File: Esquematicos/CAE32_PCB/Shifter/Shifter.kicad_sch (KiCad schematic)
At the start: 20 parts, among them J1 EXP-PORT, J2 SPI_DEVICE, J3 Conn_01x08_Female, J4 Conn_01x08_Female, J5 Conn_01x08_Female, SW1 USB_BOOT, U1 RP2040, U2 W25Q16JVSNIQ, Y1 12Mhz

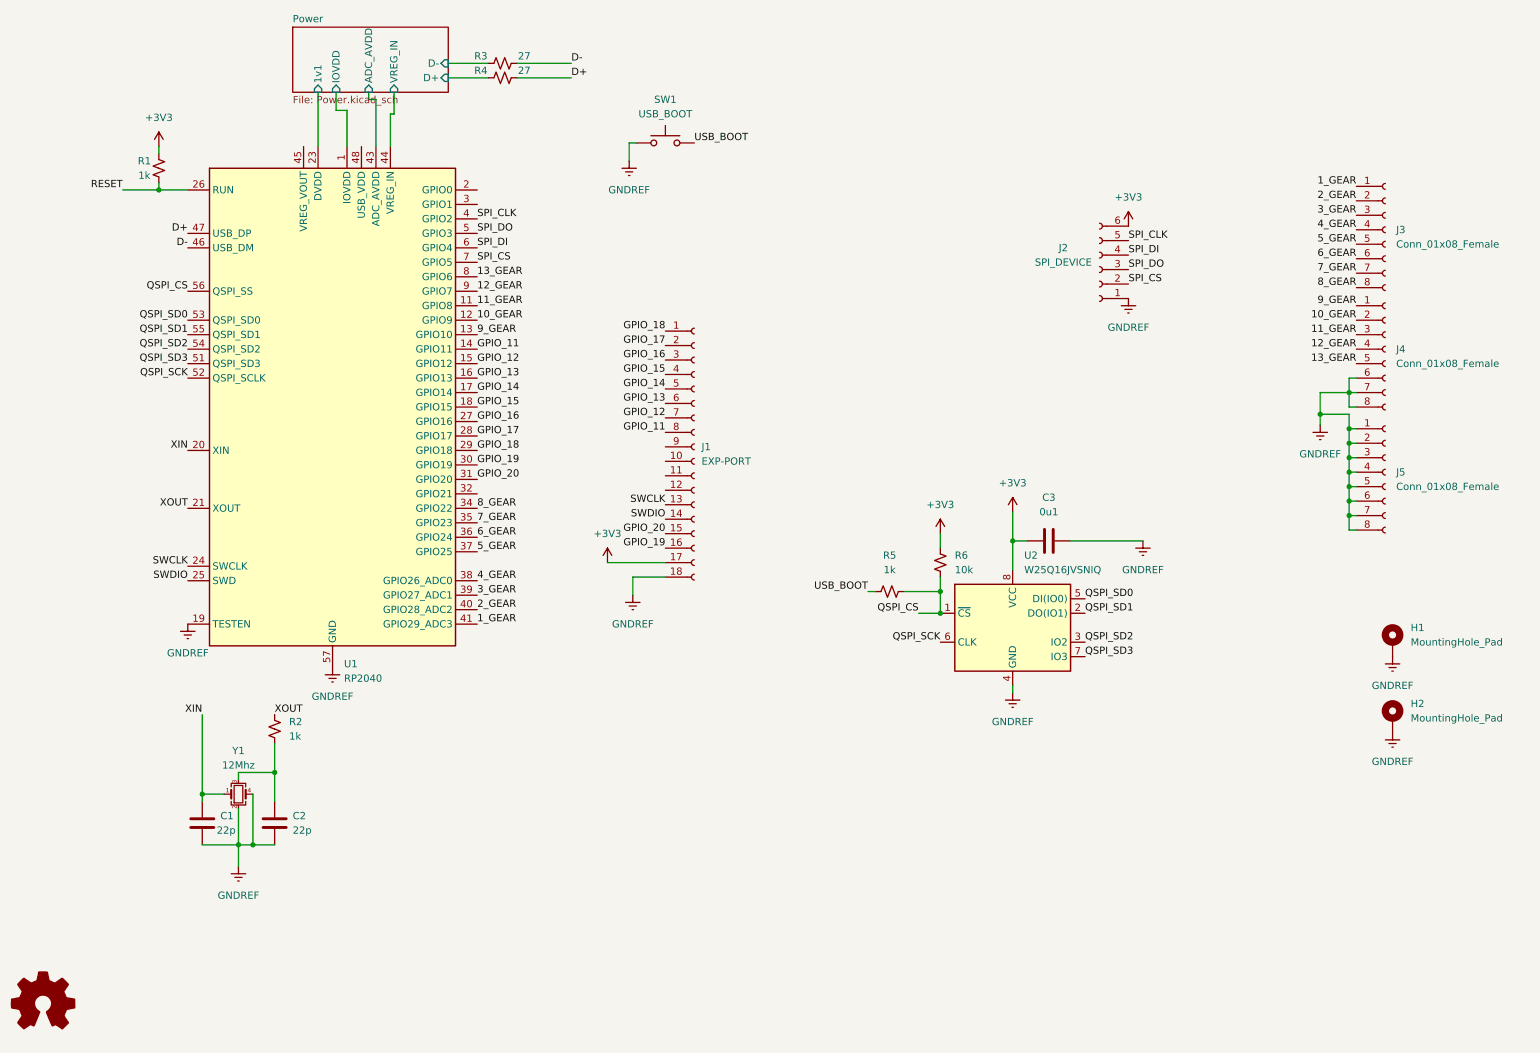
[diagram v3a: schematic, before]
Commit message: update: Se añade nombre y se separa a los diferentes componentes por categoria en el esquematico
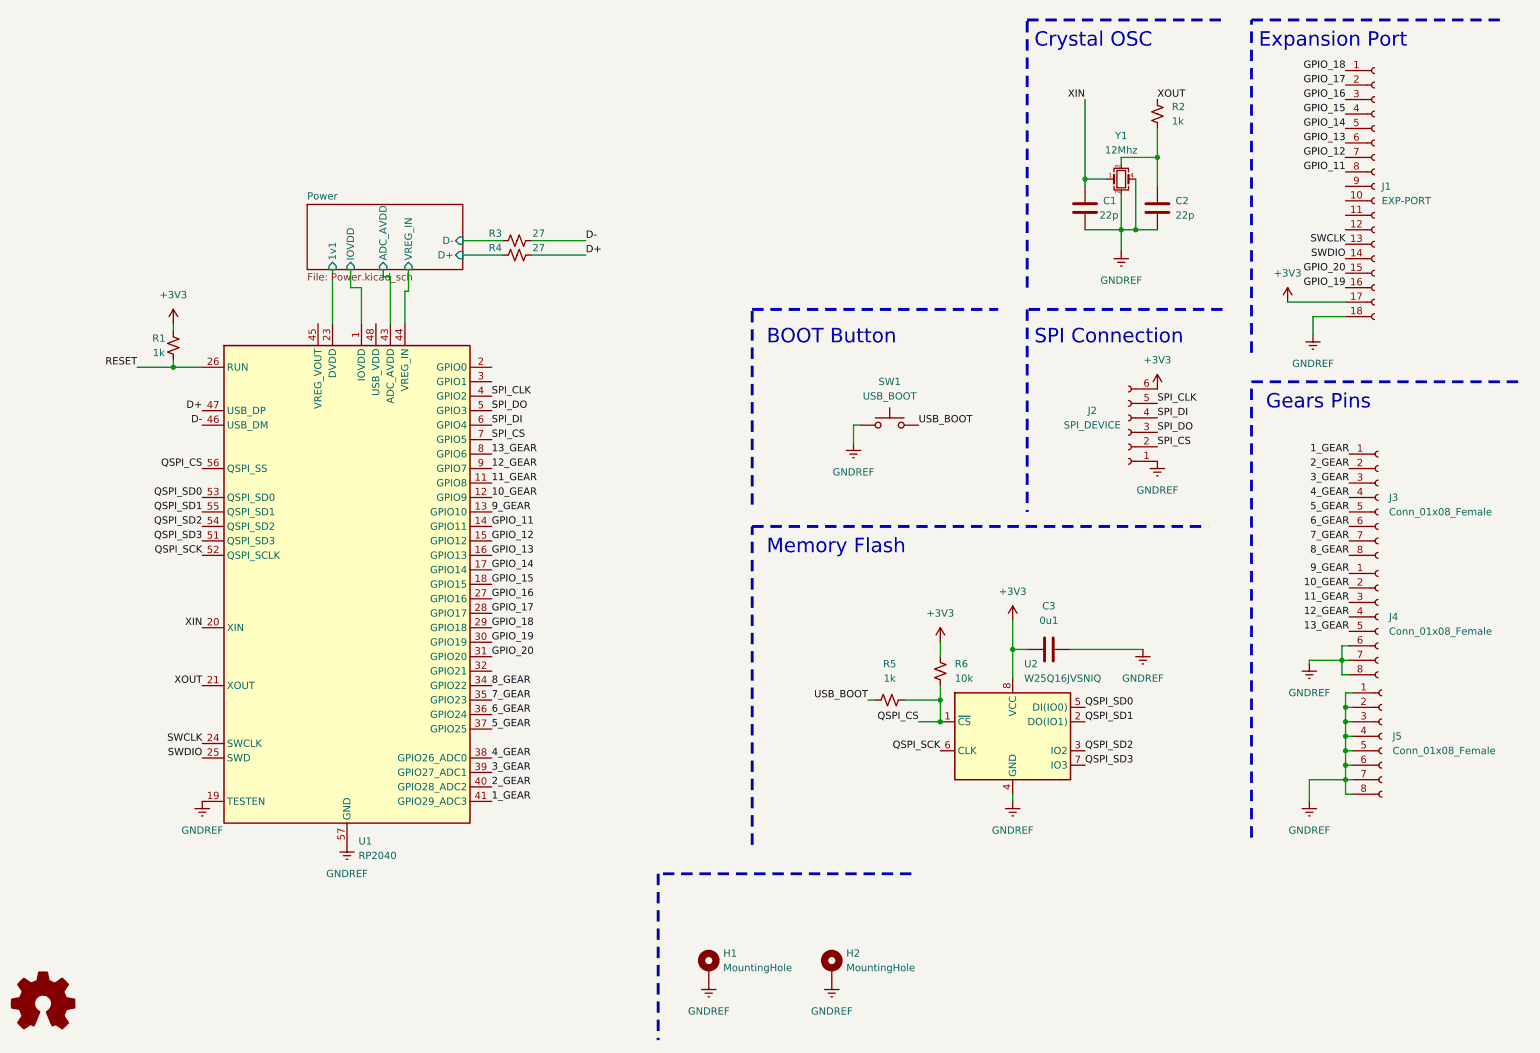
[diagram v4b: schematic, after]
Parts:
- H1, H2: value MountingHole_Pad -> MountingHole
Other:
- note added: "BOOT Button"
- note added: "Crystal OSC"
- note added: "Expansion Port"
- note added: "Gears Pins"
- note added: "Memory Flash"
- note added: "SPI Connection"
- title: (none) -> CAE32 Shifter
- moved on the sheet: C1, C2, C3, H1, H2, J1, J2, J3, J4, J5, R1, R2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

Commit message: update: changed the castelled holes for pin sockets and changed 0603 footprints to 0402
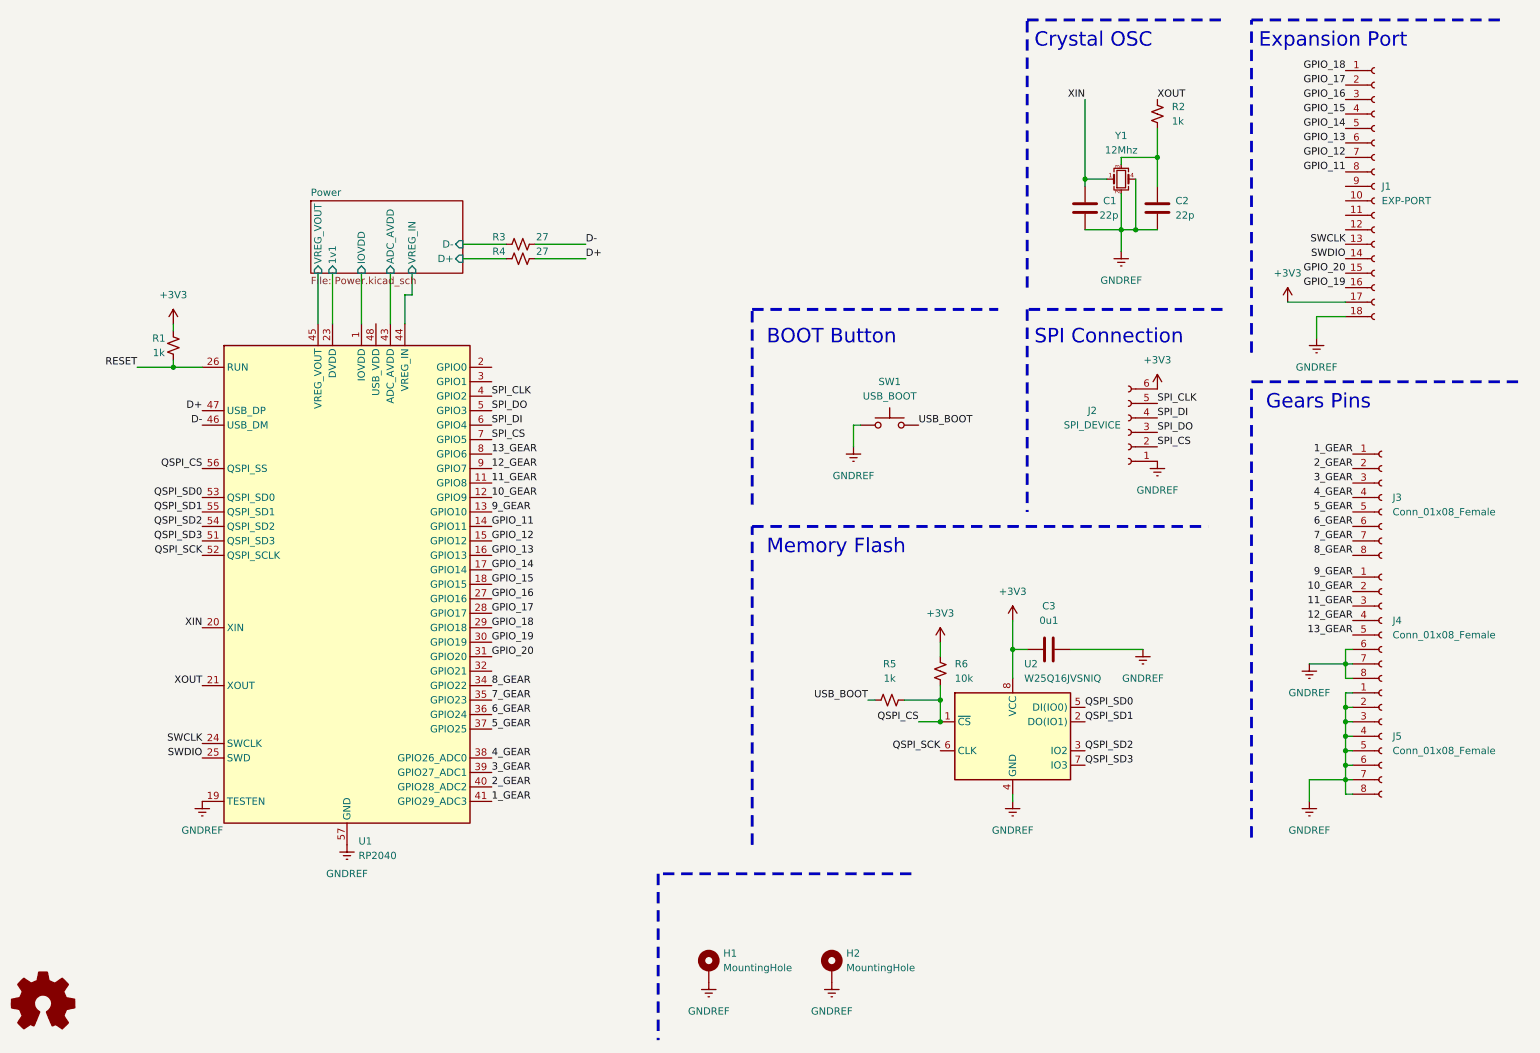
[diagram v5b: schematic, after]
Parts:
- C1, C2, C3: footprint Capacitor_SMD:C_0603_1608Metric_Pad1.08x0.95mm_HandSolder -> Capacitor_SMD:C_01005_0402Metric
- J3, J4, J5: footprint shifter:shi -> Connector_PinSocket_2.54mm:PinSocket_1x08_P2.54mm_Vertical
- R1, R2, R3, R4, R5, R6: footprint Resistor_SMD:R_0603_1608Metric_Pad0.98x0.95mm_HandSolder -> Resistor_SMD:R_0402_1005Metric
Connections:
- net Power/VREG_VOUT: now reaches U1.45 (VREG_VOUT)
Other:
- sheet Power ports: added VREG_VOUT; removed none
- moved on the sheet: J3, J4, R3, R4

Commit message: chore: arrange of schematic elements
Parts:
- C3: Vendor C42998 -> C913620
- J3, J4, J5: Vendor (none) -> C27438
- Y1: Vendor (none) -> C9002
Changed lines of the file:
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@@
+      (effects (font (size 1.27 1.27)) hide)
+    )
+    (property "Vendor" "C9002" (at 210.82 44.45 0)
       (effects (font (size 1.27 1.27)) hide)
     )
@@
       (effects (font (size 1.27 1.27)) hide)
     )
+    (property "Vendor" "C27438" (at 256.54 142.24 0)
+      (effects (font (size 1.27 1.27)) hide)
+    )
     (pin "1")
     (pin "2")
@@
       (effects (font (size 1.27 1.27)) hide)
     )
+    (property "Vendor" "C27438" (at 256.54 100.33 0)
+      (effects (font (size 1.27 1.27)) hide)
+    )
     (pin "1")
     (pin "2")
@@
       (effects (font (size 1.27 1.27)) hide)
     )
+    (property "Vendor" "C27438" (at 256.54 121.92 0)
+      (effects (font (size 1.27 1.27)) hide)
+    )
     (pin "1")
     (pin "2")
@@
       (effects (font (size 1.27 1.27)) hide)
     )
-    (property "Vendor" "C42998" (at 198.12 127 0)
-      (effects (font (size 1.27 1.27)) hide)
-    )
+    (property "Vendor" "C913620" (at 198.12 127 0)
+      (effects (font (size 1.27 1.27)) hide)
+    )

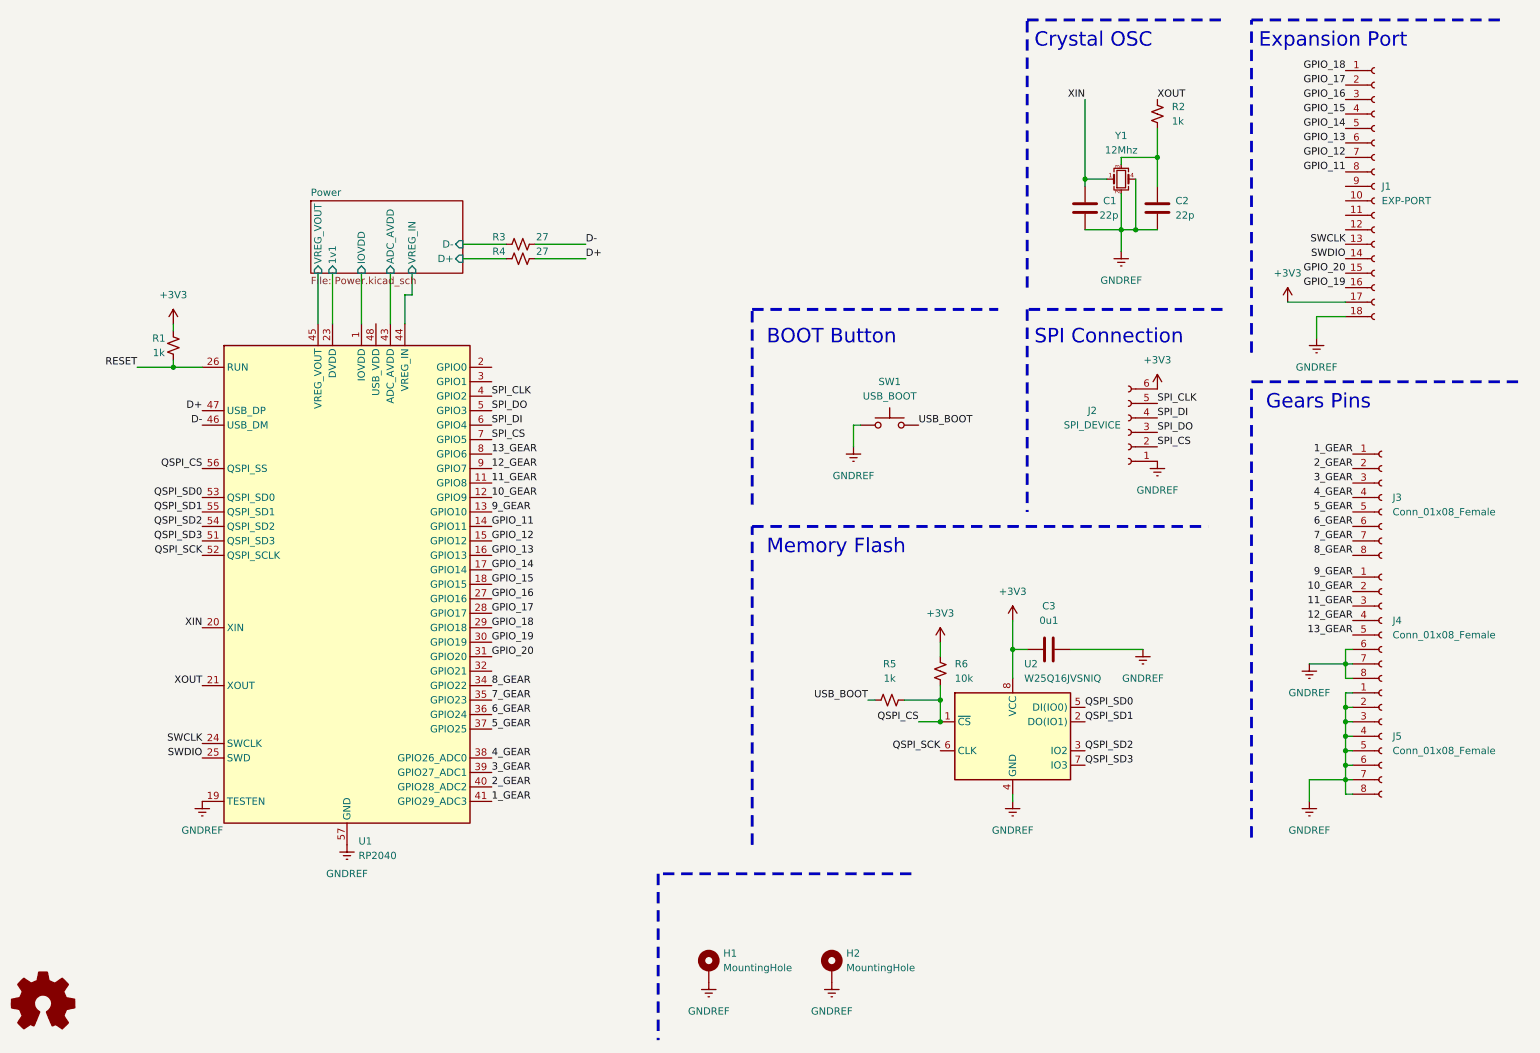
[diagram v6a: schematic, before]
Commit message: update: added minor improvements to Shifter's PCB
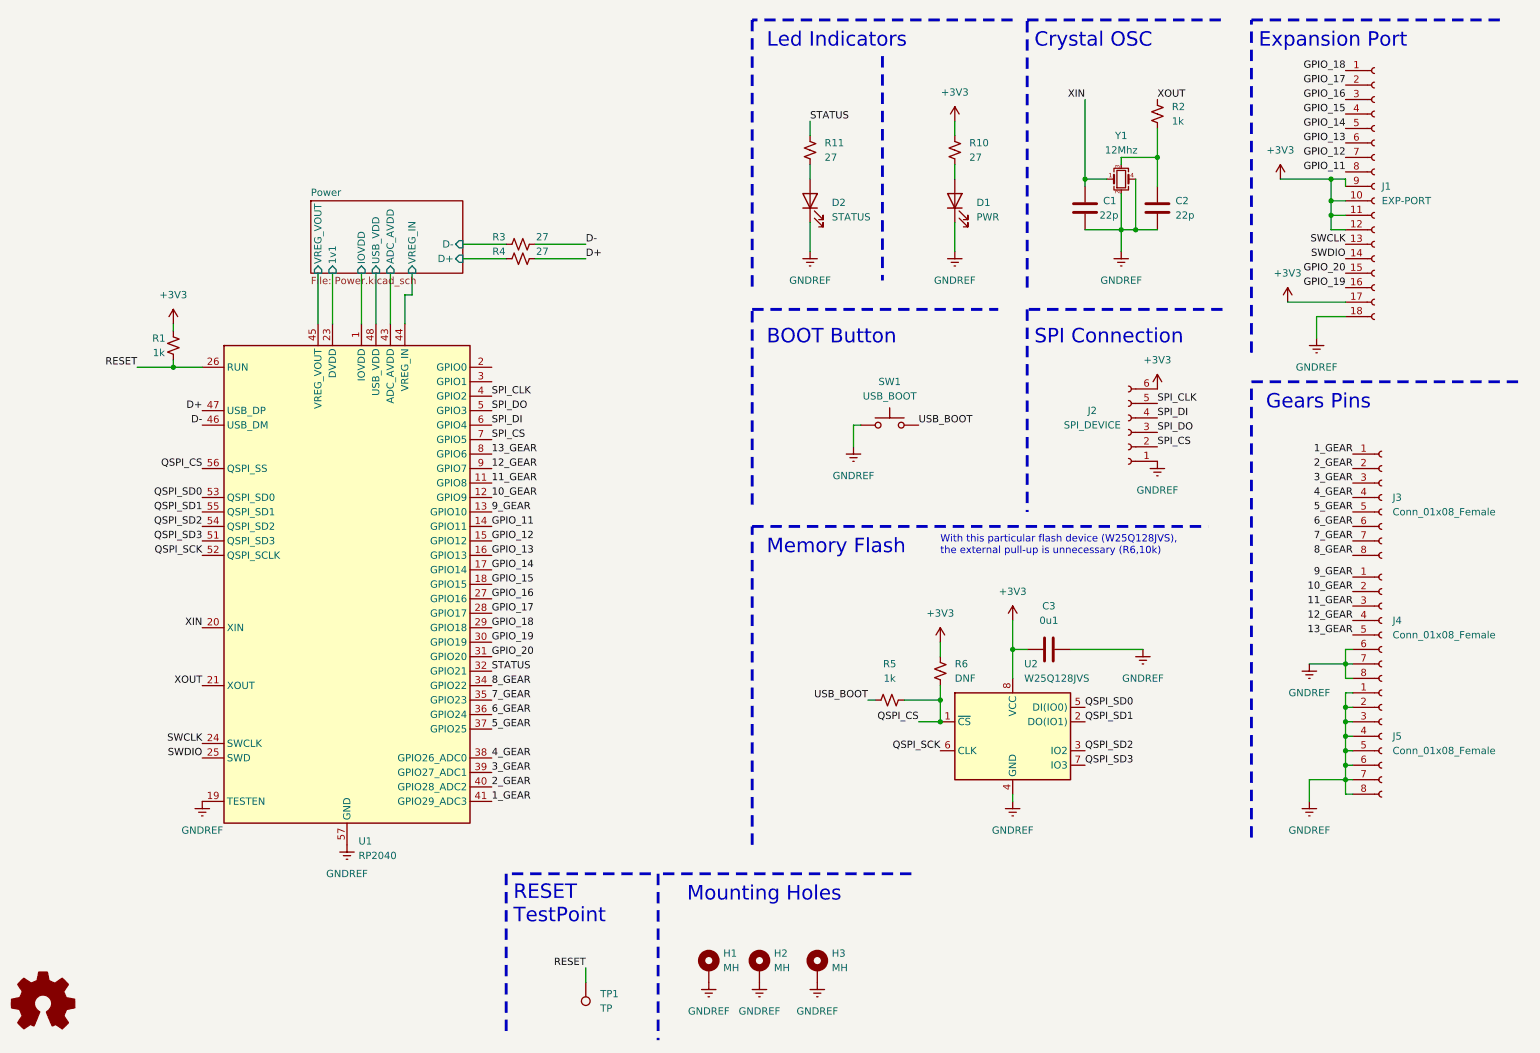
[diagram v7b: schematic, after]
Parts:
- added D1: PWR, LED_SMD:LED_0402_1005Metric, symbol Device:LED
- added D2: STATUS, LED_SMD:LED_0402_1005Metric, symbol Device:LED
- added H3: MH, MountingHole:MountingHole_2.7mm_M2.5_Pad_Via, symbol Mechanical:MountingHole_Pad
- added R10, R11: 27, Resistor_SMD:R_0402_1005Metric, symbol Device:R_Small_US
- added TP1: TP, TestPoint:TestPoint_Pad_D1.0mm, symbol Connector:TestPoint
- H1, H2: value MountingHole -> MH
- R6: value 10k -> DNF
- U2: value W25Q16JVSNIQ -> W25Q128JVS; Vendor C2456211 -> C97521
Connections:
- net +3V3: now also J1.10 (Pin_10), J1.11 (Pin_11), J1.12 (Pin_12), J1.9 (Pin_9), R10.1
- net GNDREF: now also D1.1 (K), D2.1 (K), H3.1
- net RESET: now also TP1.1
- net STATUS: now reaches U1.32 (GPIO21)
- net STATUS: now also R11.1
- net Power/USB_VDD: now reaches U1.48 (USB_VDD)
- new net: D2.2 (A), R11.2
- new net: D1.2 (A), R10.2
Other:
- sheet Power ports: added USB_VDD; removed none
- note added: "Led Indicators"
- note added: "Mounting Holes"
- note added: "RESET TestPoint"
- note added: "With this particular flash device (W25Q128JVS), the external pull-up is unnecessary (R6,10k)"
- moved on the sheet: H2
